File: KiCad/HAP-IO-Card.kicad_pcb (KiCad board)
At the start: 2 copper layers, 110 x 72 mm, 419 parts, among them CON601 AVR-JTAG-10, J201 TE_Connectivity_1-282834-0, J202 TE_Connectivity_282834-6, J203 GS3, J204 GS3, J205 GS3, J206 GS3, J207 GS3, J208 GS3, J209 GS3, J210 GS3, J211 TE_Connectivity_282834-6, J212 TE_Connectivity_1-282834-0, J401 TE_Connectivity_1-282834-0, J402 TE_Connectivity_282834-6, J501 TE_Connectivity_282834-3, J502 CONN_01X03_FEMALE, J601 ISP0, J602 ISP1, J603 CONN_01X02, J604 CONN_01X02, J605 CONN_01X02, J606 CONN_01X02, J607 CONN_01X03, J608 CONN_01X03, J701 5V_I/O_2, J702 5V_I/O_1, J703 NEO1, J704 NEO2, J705 NEO3, J706 NEO4, J707 CONN_01X03, Q201 ZXTN25050DFHTA, Q202 ZXTN25050DFHTA, Q203 ZXTN25050DFHTA, Q204 ZXTN25050DFHTA, Q205 ZXTN25050DFHTA, Q206 ZXTN25050DFHTA, Q207 ZXTN25050DFHTA, Q208 ZXTN25050DFHTA, U201 LTV-354T, U202 LTV-354T, U203 LTV-354T, U204 LTV-354T, U205 LTV-354T, U206 LTV-354T, U207 LTV-354T, U208 LTV-354T, U209 MCP23017, U401 ADS1115IDGST, U402 ADS1115IDGST, U501 LM1086-5V, U502 LM1086-3.3V, U701 TXB0102DCT

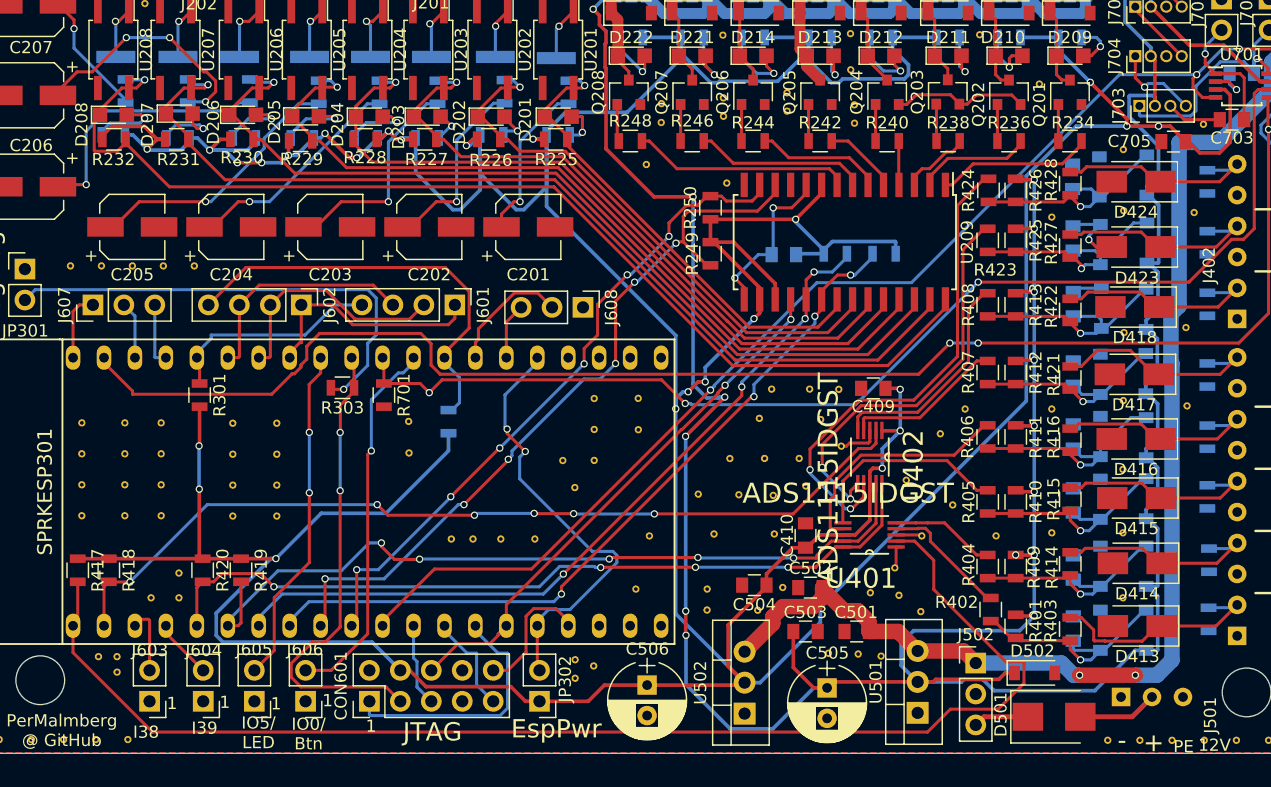
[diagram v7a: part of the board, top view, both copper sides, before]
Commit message: Increased width of 3.3V rail
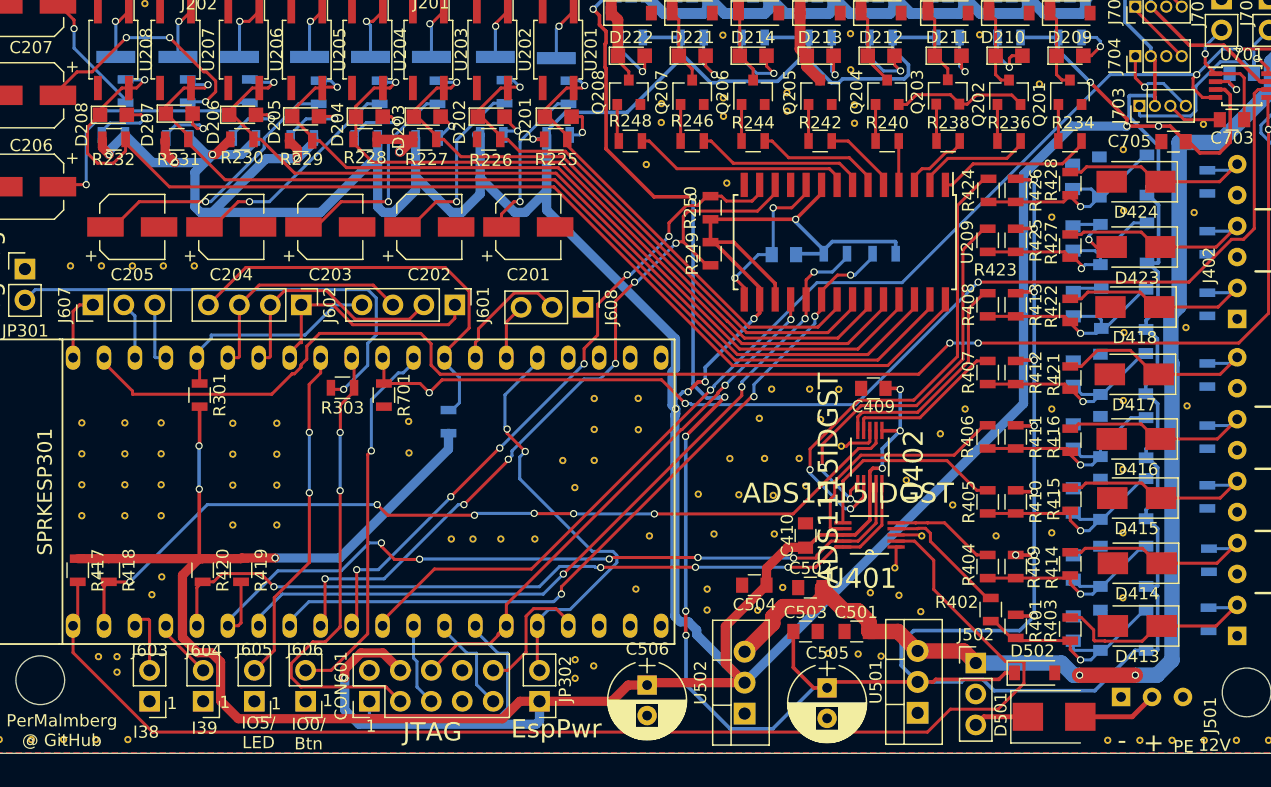
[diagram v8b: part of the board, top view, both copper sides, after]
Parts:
- removed the REF** at (54.6, 76.7)
- moved REF** 1.44 mm to (53.2, 75.0)
- moved REF** 0.73 mm to (62.6, 70.7)
- moved REF** 0.73 mm to (59.0, 70.7)
- moved REF** 0.27 mm to (52.4, 76.5)
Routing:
- net POWER3V3: track 470.8 -> 529.3 mm, vias 25 -> 21
- net DI8: track 90.5 -> 92.6 mm
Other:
- net class 3V3: trace_width 0.3 -> 0.76
